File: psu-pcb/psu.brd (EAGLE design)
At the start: 100 x 80 mm, 0 parts

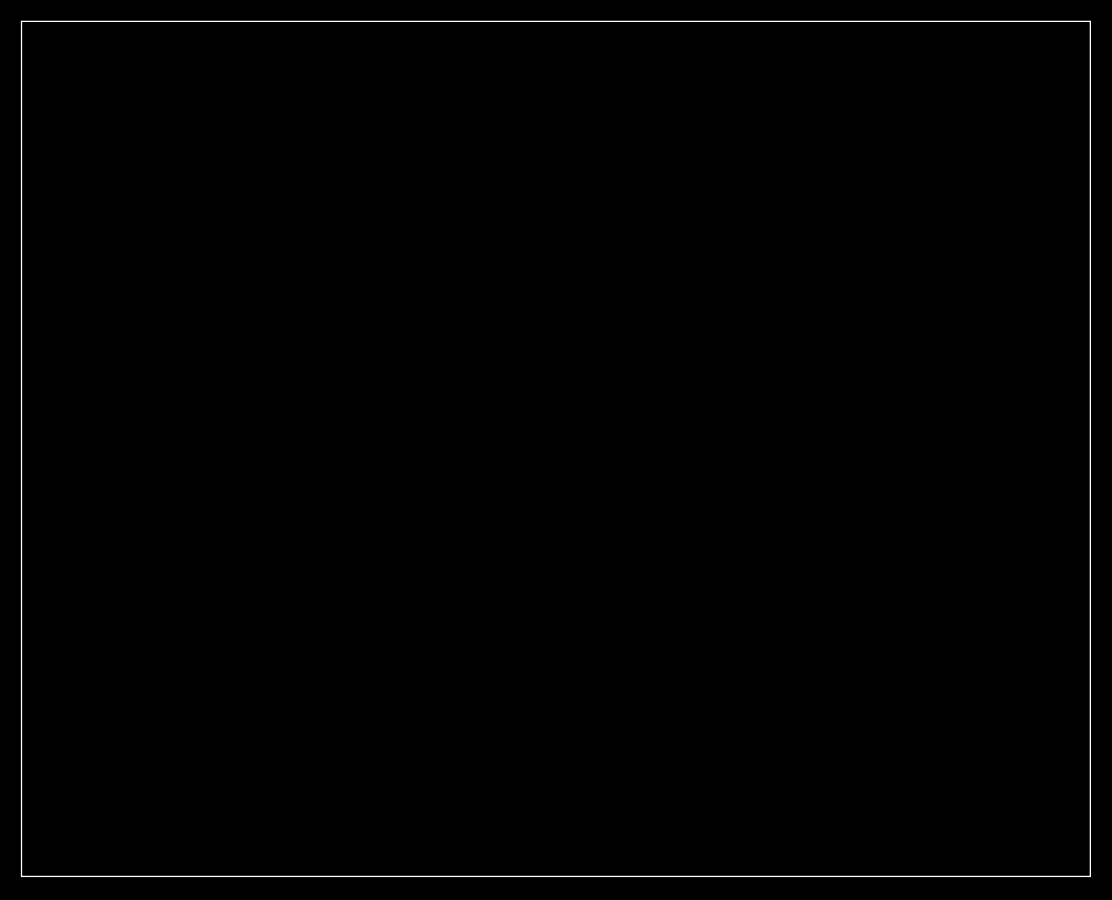
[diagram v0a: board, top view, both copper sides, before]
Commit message: Updated board and layout, and updated gitignore
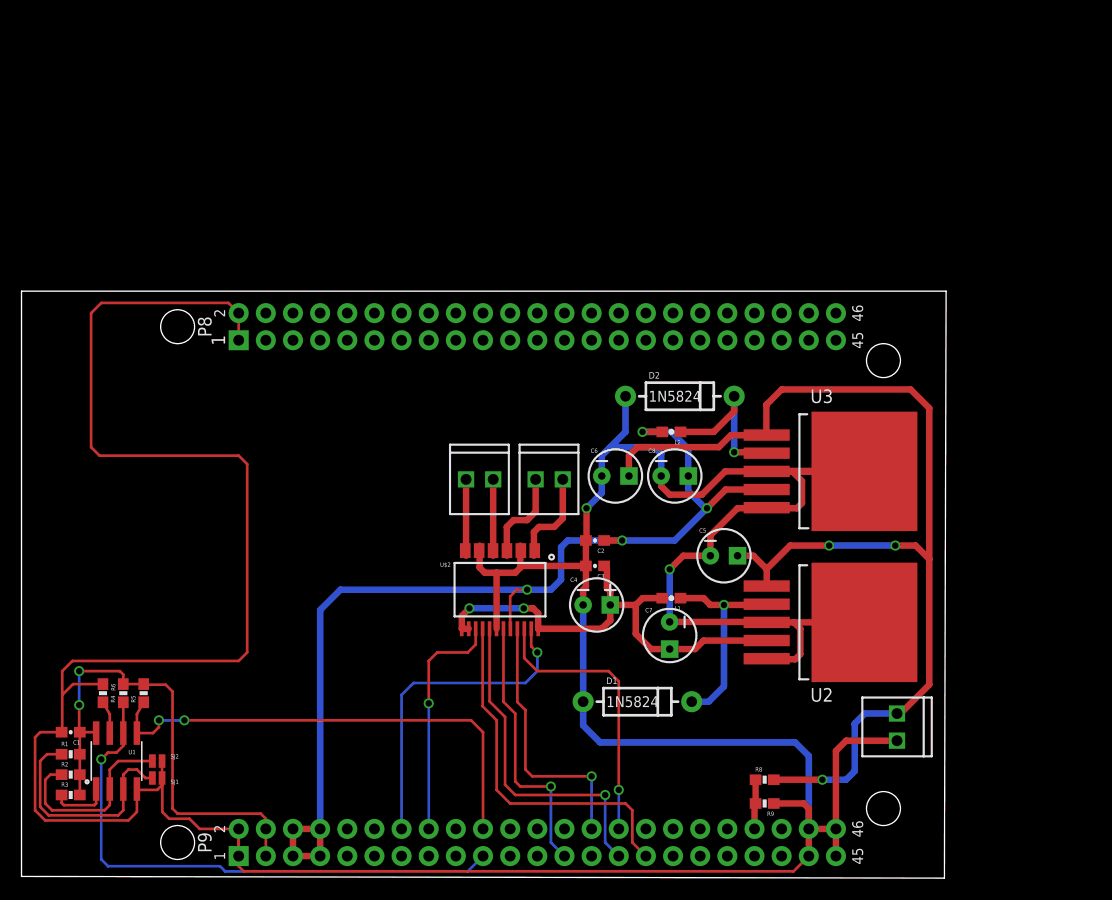
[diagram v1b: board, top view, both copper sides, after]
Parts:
- added C1, C2, C3: 0.1uF, SparkFun-Capacitors:0603-CAP
- added C4: (no value), SparkFun-Capacitors:CPOL-RADIAL-10UF-25V-KIT
- added C5: 680uF, SparkFun-Capacitors:CPOL-RADIAL-10UF-25V
- added C6: 680 uF, SparkFun-Capacitors:CPOL-RADIAL-10UF-25V
- added C7: 220uF, SparkFun-Capacitors:CPOL-RADIAL-10UF-25V
- added C8: 220 uF, SparkFun-Capacitors:CPOL-RADIAL-10UF-25V
- added D1, D2: 1N5824, SparkFun-DiscreteSemi:DIODE-1N4001
- added FRAME2: FRAME-LEDGER, SparkFun-Aesthetics:CREATIVE_COMMONS
- added JP1, JP2, JP3: (no value), SparkFun-Connectors:1X02_2.54_SCREWTERM
- added L1, L2: 33 uH, SparkFun-Passives:0603
- added R1, R2, R3, R4, R5: 4.7K, SparkFun-Resistors:0603-RES
- added R6, R8, R9: 10K, SparkFun-Resistors:0603-RES
- added SJ1, SJ2: JUMPER-PAD-2-NO, SparkFun-Passives:PAD-JUMPER-2-NO_NO_SILK
- added U$1: BEAGLE_BONE_BLACK_CAPE, SparkFun-Boards:BEAGLE_BONE_BLACK_CAPE
- added U$2: TB6612FNG, SparkFun-PowerIC:SSOP24
- added U1: EEPROM-I2CSMD, SparkFun-DigitalIC:SO08
- added U2, U3: LM2596, psu:TO-263
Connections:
- new net 3.3V: C1.1, R1.2, R2.2, R3.2, R4.2, R5.2, U$1.P9.3, U$1.P9.4, U1.8
- new net A01: JP2.P1, U$2.1, U$2.2
- new net A02: JP2.P2, U$2.5, U$2.6
- new net AIN1: U$1.P9.28, U$2.21
- new net AIN2: U$1.P9.30, U$2.22
- new net B01: JP3.P2, U$2.11, U$2.12
- new net B02: JP3.P1, U$2.7, U$2.8
- new net BIN1: U$1.P9.29, U$2.17
- new net BIN2: U$1.P9.31, U$2.16
- new net GND: C1.2, C2.2, C3.2, C4.2, C5.2, C6.2, C7.2, C8.2, D1.A, D2.A, JP1.P1, R6.1, R9.1, SJ1.1, SJ2.1, U$1.P8.1, U$1.P8.2, U$1.P9.1, U$1.P9.2, U$1.P9.43, U$1.P9.44, U$1.P9.45, U$1.P9.46, U$2.10, U$2.18, U$2.3, U$2.4, U$2.9, U1.4, U2.3, U2.5, U2.6, U3.3, U3.5, U3.6
- new net N$1: R3.1, U1.1
- new net N$2: R2.1, SJ2.2, U1.2
- new net N$3: R1.1, SJ1.2, U1.3
- new net N$4: R8.1, R9.2, U$1.P9.40
- new net N$5: R6.2, U1.7
- new net N$6: U$1.P9.15
- new net N$7: U$1.P9.13
- new net N$8: D1.C, L1.1, U2.2
- new net N$9: D2.C, L2.1, U3.2
- new net PWMA: U$1.P9.14, U$2.23
- new net PWMB: U$1.P9.16, U$2.15
- new net SCL: R4.1, U$1.P9.19, U1.6
- new net SDA: R5.1, U$1.P9.20, U1.5
- new net STBY: U$1.P9.25, U$2.19
- new net V_BATT: C5.1, C6.1, JP1.P2, R8.2, U2.1, U3.1
- new net V_CPU: C2.1, C8.1, L2.2, U$1.P9.5, U$1.P9.6, U$1.P9.7, U$1.P9.8, U$2.20, U3.4
- new net V_MOTOR: C3.1, C4.1, C7.1, L1.2, U$2.13, U$2.14, U$2.24, U2.4
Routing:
- net GND: track 0.00 -> 399.5 mm, vias 0 -> 2
- net V_BATT: track 0.00 -> 103.2 mm, vias 0 -> 3
- net V_CPU: track 0.00 -> 98.6 mm, vias 0 -> 4
- net SCL: track 0.00 -> 52.8 mm, vias 0 -> 1
- net 3.3V: track 0.00 -> 47.0 mm, vias 0 -> 2
- net SDA: track 0.00 -> 45.8 mm, vias 0 -> 2
- net V_MOTOR: track 0.00 -> 44.5 mm, vias 0 -> 2
- net BIN2: track 0.00 -> 33.9 mm
- net BIN1: track 0.00 -> 31.2 mm, vias 0 -> 1
- net PWMA: track 0.00 -> 30.4 mm, vias 0 -> 1
- net AIN2: track 0.00 -> 26.3 mm, vias 0 -> 1
- net STBY: track 0.00 -> 25.3 mm, vias 0 -> 1
- net AIN1: track 0.00 -> 24.9 mm, vias 0 -> 1
- net PWMB: track 0.00 -> 22.2 mm, vias 0 -> 1
- net N$3: track 0.00 -> 21.4 mm
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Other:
- board size 100 x 80 mm -> 86.5 x 54.9 mm

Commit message: Fixed board outline
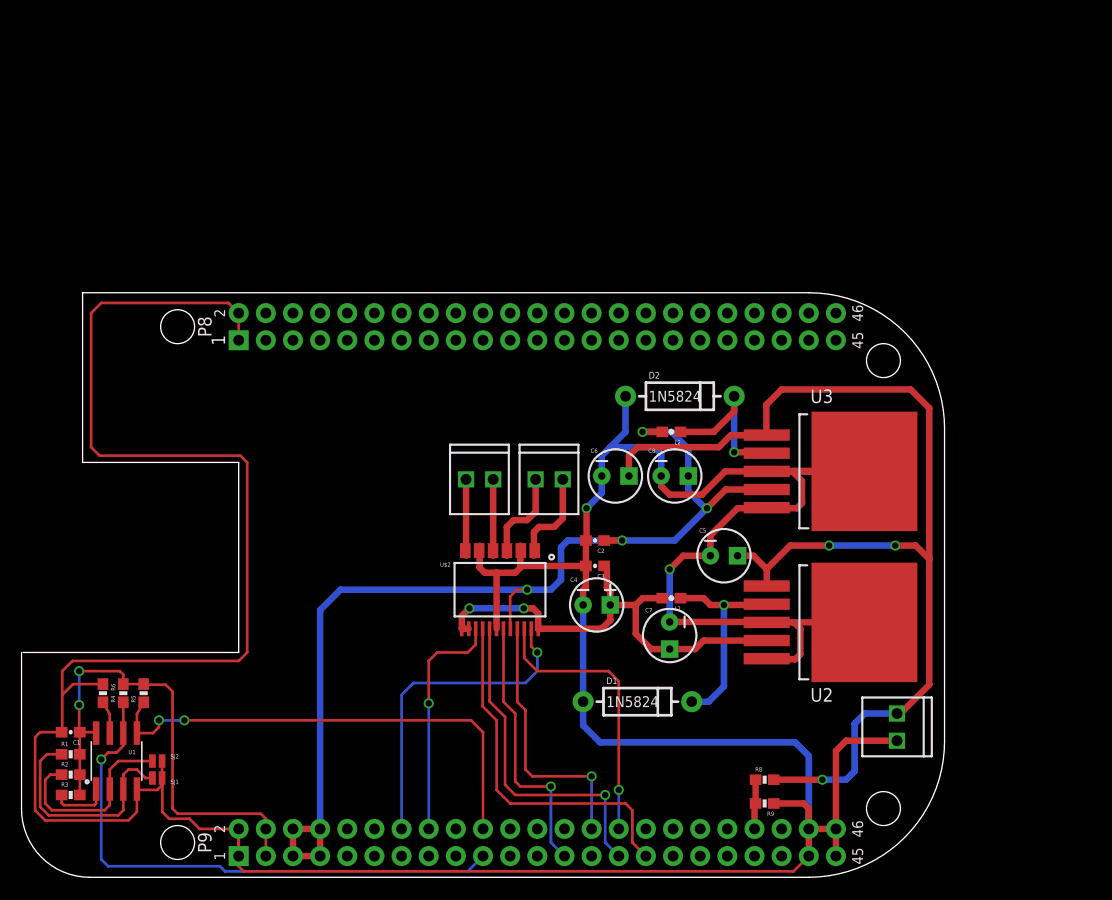
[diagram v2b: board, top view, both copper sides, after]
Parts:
- C4: value (none) -> 10uF, 20V
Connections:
- removed net N$6: U$1.P9.15
- removed net N$7: U$1.P9.13
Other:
- board size 86.5 x 54.9 mm -> 86.4 x 54.7 mm
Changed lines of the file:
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@@
 <board>
 <plain>
-<wire x1="0" y1="0" x2="86.3475" y2="-0.15875" width="0" layer="20"/>
-<wire x1="86.3475" y1="-0.15875" x2="86.50625" y2="54.75875" width="0" layer="20"/>
-<wire x1="86.50625" y1="54.75875" x2="0" y2="54.75875" width="0" layer="20"/>
-<wire x1="0" y1="54.75875" x2="0" y2="0" width="0" layer="20"/>
+<wire x1="0" y1="20.955" x2="0" y2="6.34404375" width="0.0254" layer="20"/>
+<wire x1="0" y1="6.34404375" x2="6.34404375" y2="-0.079375" width="0.0254" layer="20" curve="90"/>
+<wire x1="6.34404375" y1="-0.079375" x2="73.678865625" y2="-0.079375" width="0.0254" layer="20"/>
+<wire x1="73.678865625" y1="-0.079375" x2="86.36" y2="12.681134375" width="0.0254" layer="20" curve="90"/>
+<wire x1="86.36" y1="12.681134375" x2="86.36" y2="41.92489375" width="0.0254" layer="20"/>
+<wire x1="86.36" y1="41.92489375" x2="73.67489375" y2="54.61" width="0.0254" layer="20" curve="90"/>
+<wire x1="73.67489375" y1="54.61" x2="5.715" y2="54.61" width="0.0254" layer="20"/>
+<wire x1="5.715" y1="54.61" x2="5.715" y2="38.735" width="0.0254" layer="20"/>
+<wire x1="5.715" y1="38.735" x2="20.32" y2="38.735" width="0.0254" layer="20"/>
+<wire x1="20.32" y1="38.735" x2="20.32" y2="20.955" width="0.0254" layer="20"/>
+<wire x1="20.32" y1="20.955" x2="0.15875" y2="20.955" width="0.0254" layer="20"/>
 </plain>
 <attributes>
@@
 <attribute name="NAME" x="14.71925" y="11.43" size="0.4064" layer="25" rot="R180"/>
 </element>
-<element name="U$1" library="SparkFun-Boards" package="BEAGLE_BONE_BLACK_CAPE" value="BEAGLE_BONE_BLACK_CAPE" x="0" y="0"/>
+<element name="U$1" library="SparkFun-Boards" package="BEAGLE_BONE_BLACK_CAPE" value="BEAGLE_BONE_BLACK_CAPE" x="0" y="0" smashed="yes">
+<attribute name="VALUE" x="19.05" y="-1.27" size="1.27" layer="48" font="vector" ratio="15" align="center-left"/>
+<attribute name="NAME" x="19.05" y="55.88" size="1.27" layer="48" font="vector" ratio="15" align="center-left"/>
+</element>
 <element name="U2" library="psu" package="TO-263" value="LM2596" x="83.82" y="29.36875" smashed="yes" rot="R270">
 <attribute name="NAME" x="73.80125" y="16.35125" size="1.27" layer="21"/>
@@
 <attribute name="PROD_ID" value="CAP-00810" x="53.6575" y="29.05125" size="1.778" layer="27" rot="R180" display="off"/>
 </element>
-<element name="C4" library="SparkFun-Capacitors" package="CPOL-RADIAL-10UF-25V-KIT" value="" x="53.81625" y="25.4" smashed="yes">
+<element name="C4" library="SparkFun-Capacitors" package="CPOL-RADIAL-10UF-25V-KIT" value="10uF, 20V" x="53.81625" y="25.4" smashed="yes">
 <attribute name="PROD_ID" value="CAP-08440" x="53.81625" y="25.4" size="1.778" layer="27" display="off"/>
 <attribute name="NAME" x="51.33975" y="27.559" size="0.4064" layer="25"/>
@@
 <wire x1="6.50875" y1="52.705" x2="6.50875" y2="40.16375" width="0.254" layer="1"/>
 <wire x1="6.50875" y1="40.16375" x2="7.3025" y2="39.37" width="0.254" layer="1"/>
-<wire x1="7.3025" y1="39.37" x2="20.32" y2="39.37" width="0.254" layer="1"/>
-<wire x1="20.32" y1="39.37" x2="21.11375" y2="38.57625" width="0.254" layer="1"/>
-<wire x1="21.11375" y1="38.57625" x2="21.11375" y2="20.955" width="0.254" layer="1"/>
+<wire x1="7.3025" y1="39.37" x2="20.47875" y2="39.37" width="0.254" layer="1"/>
+<wire x1="20.47875" y1="39.37" x2="21.11375" y2="38.735" width="0.254" layer="1"/>
+<wire x1="21.11375" y1="38.735" x2="21.11375" y2="20.955" width="0.254" layer="1"/>
 <wire x1="21.11375" y1="20.955" x2="20.32" y2="20.16125" width="0.254" layer="1"/>
 <wire x1="20.32" y1="20.16125" x2="4.7625" y2="20.16125" width="0.254" layer="1"/>
@@
 <wire x1="36.67125" y1="18.0975" x2="36.433125" y2="17.859375" width="0.254" layer="16"/>
 </signal>
-<signal name="N$6">
-<contactref element="U$1" pad="P9.15"/>
-</signal>
-<signal name="N$7">
-<contactref element="U$1" pad="P9.13"/>
-</signal>
 <signal name="N$8">
